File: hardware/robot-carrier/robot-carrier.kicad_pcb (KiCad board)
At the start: 2 copper layers, 65.5 x 73.5 mm, 36 parts, among them J1 DB128L BAT IN, LCSC C500021, J10 M1, J11 M2, J12 M3, J13 M4, J2 DB128L 2P, LCSC C500021, J20 S1, J21 S2, J22 S3, J23 S4, J3 DB128L 2P, LCSC C500021, J30 IMU I2C, J40 GA25-370 L298N: ENA / IN1 / I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, J41 DB128L 3P, LCSC C430602

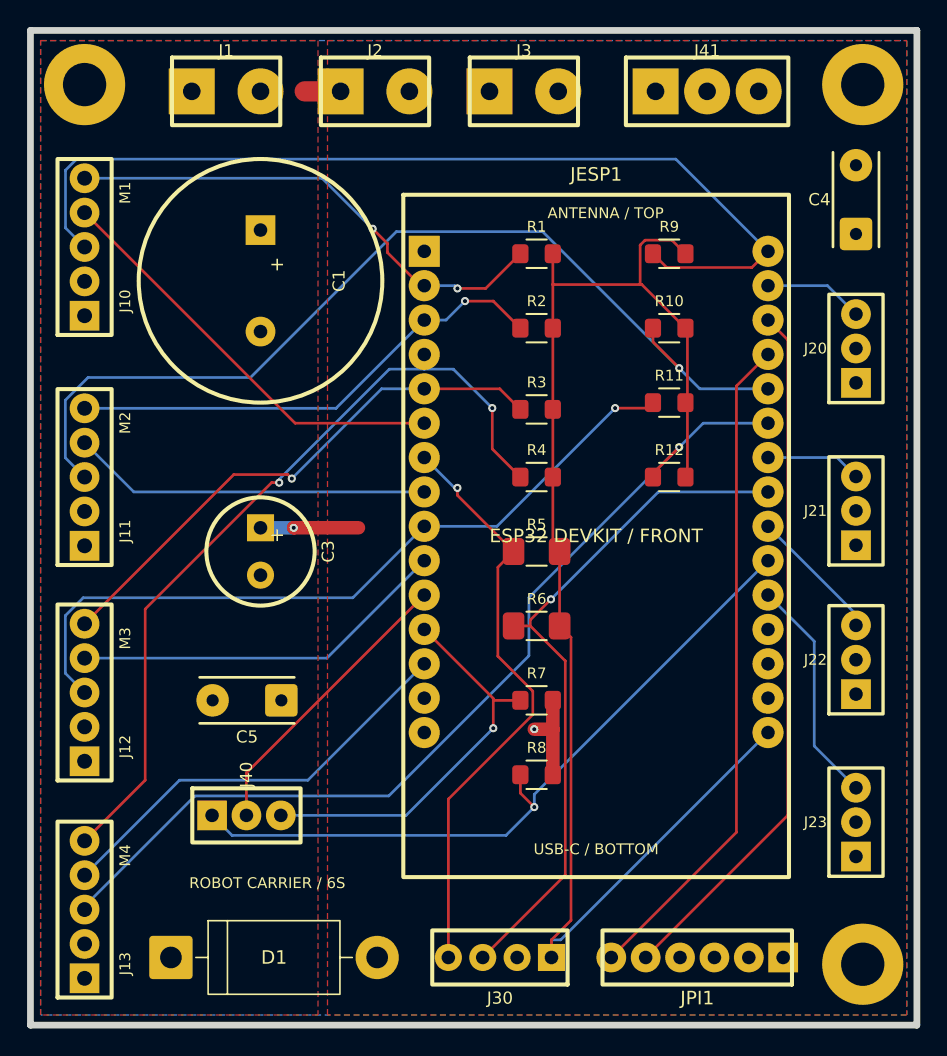
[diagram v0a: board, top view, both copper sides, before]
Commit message: Route carrier board with 1mm power and ground
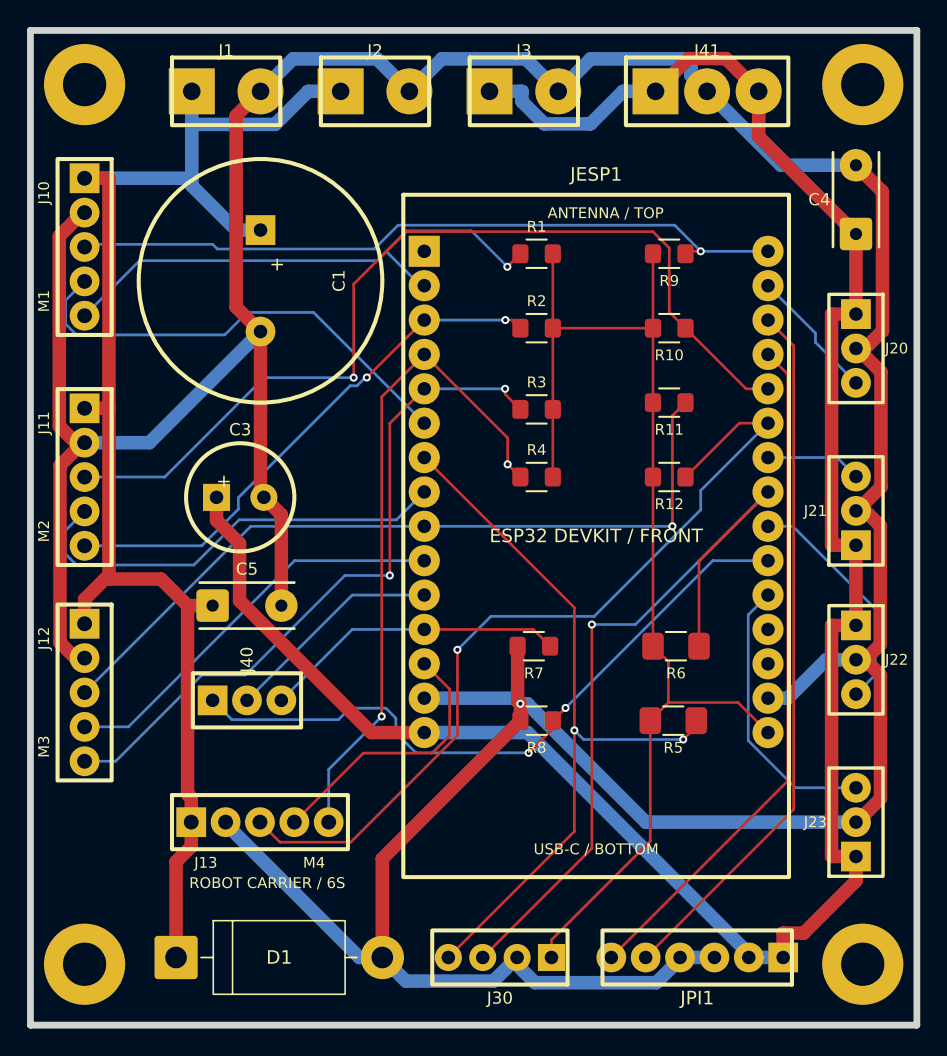
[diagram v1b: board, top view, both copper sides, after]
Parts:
- added H4: M3, Custom:MountingHole_M3, F.Cu at (24.0, 89.0)
- moved R5 16.1 mm to (67.5, 71.0), turned to 180 degrees
- moved J13 14.5 mm to (37.0, 78.5), turned to 0 degrees
- moved R6 10.4 mm to (67.7, 65.5), turned to 180 degrees
- moved J40 8.50 mm to (36.0, 69.5)
- moved C5 7.00 mm to (36.0, 62.5), turned to 0 degrees
- moved C3 4.27 mm to (35.5, 54.5), turned to 0 degrees
- moved R7 4.00 mm to (57.2, 65.5), turned to 180 degrees
- moved R8 4.00 mm to (57.4, 71.0), turned to 180 degrees
- moved D1 0.38 mm to (30.8, 88.5)
- turned J10 to -90 degrees
- turned J11 to -90 degrees
- turned J12 to -90 degrees
- turned J20 to -90 degrees
- turned J22 to -90 degrees
- turned R10 to 180 degrees
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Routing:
- net GND: track 6.87 -> 315.2 mm
- net +5V: track 7.24 -> 161.2 mm, vias 1 -> 0
- net VIN_PROTECTED: track 2.65 -> 105.8 mm
- net +3V3: track 106.0 -> 88.2 mm
- net M1_PWM_3V3: track 70.7 -> 53.5 mm, vias 0 -> 1
- net IMU_I2C_SDA_3V3: track 43.9 -> 55.5 mm, vias 1 -> 2
- net M4_DIR_3V3: track 31.6 -> 20.2 mm
- net M4_ENC: track 60.3 -> 49.5 mm
- net M3_ENC: track 40.3 -> 51.1 mm, vias 1 -> 2
- net M4_PWM_3V3: track 71.1 -> 63.3 mm
- net S3_PWM: track 10.0 -> 17.3 mm
- net IMU_I2C_SCL_3V3: track 51.3 -> 58.5 mm
- net GA25_IN2_3V3: track 29.8 -> 22.5 mm, vias 1 -> 0
- net M2_DIR_3V3: track 26.6 -> 32.8 mm
- net GA25_IN1_3V3: track 21.7 -> 16.3 mm
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- removed copper zone on F.Cu, net +5V
- removed copper zone on B.Cu, net GND
- removed copper zone on F.Cu, net VIN_PROTECTED

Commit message: updated to none cropper pour
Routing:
- net M4_ENC: vias 2 -> 1
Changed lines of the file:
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@@
 			(at 0 -3 0)
 			(layer "F.SilkS")
+			(hide yes)
 			(effects
 				(font
@@
 			(at 0 -3 0)
 			(layer "F.SilkS")
+			(hide yes)
 			(effects
 				(font
@@
 		)
 		(duplicate_pad_numbers_are_jumpers no)
-		(fp_rect
-			(start -4 -2.5)
-			(end 4 2.5)
-			(stroke
-				(width 0.3)
-				(type default)
-			)
-			(fill no)
-			(layer "F.SilkS")
-		)
 		(pad "1" thru_hole rect
 			(at -2.54 0)
@@
 			(at 0 -3 0)
 			(layer "F.SilkS")
+			(hide yes)
 			(effects
 				(font
@@
 		)
 		(duplicate_pad_numbers_are_jumpers no)
-		(fp_rect
-			(start -4 -2.5)
-			(end 4 2.5)
-			(stroke
-				(width 0.3)
-				(type default)
-			)
-			(fill no)
-			(layer "F.SilkS")
-		)
 		(pad "1" thru_hole rect
 			(at -2.54 0)
@@
 			(at 0 -3 0)
 			(layer "F.SilkS")
+			(hide yes)
 			(effects
 				(font
@@
 			(at 0 -3 0)
 			(layer "F.SilkS")
+			(hide yes)
 			(effects
 				(font
@@
 			(at 0 -3 0)
 			(layer "F.SilkS")
+			(hide yes)
 			(effects
 				(font
@@
 		)
 		(duplicate_pad_numbers_are_jumpers no)
-		(fp_rect
-			(start -4 -2.5)
-			(end 4 2.5)
-			(stroke
-				(width 0.3)
-				(type default)
-			)
-			(fill no)
-			(layer "F.SilkS")
-		)
 		(pad "1" thru_hole rect
 			(at -2.54 0)
@@
 			(layer "F.SilkS")
 		)
-		(fp_rect
-			(start -14.5 -22.21)
-			(end 14.5 28.71)
-			(stroke
-				(width 0.05)
-				(type default)
-			)
-			(fill no)
-			(layer "F.CrtYd")
-		)
 		(fp_text user "USB-C / BOTTOM"
 			(at 0 26.4 0)
@@
 			(at 0 -3 0)
 			(layer "F.SilkS")
+			(hide yes)
 			(effects
 				(font
@@
 		)
 		(fp_text user "+"
-			(at -1.2 -1.2 0)
+			(at -1.2 -2.7 0)
 			(layer "F.SilkS")
 			(effects
@@
 		)
 		(duplicate_pad_numbers_are_jumpers no)
-		(fp_rect
-			(start -7 -2)
-			(end 7 2)
-			(stroke
-				(width 0.3)
-				(type default)
-			)
-			(fill no)
-			(layer "F.SilkS")
-		)
 		(pad "1" thru_hole rect
 			(at -6.35 0 90)
@@
 			(at 0 -3 90)
 			(layer "F.SilkS")
+			(hide yes)
 			(effects
 				(font
@@
 			(at 0 -3 0)
 			(layer "F.SilkS")
+			(hide yes)
 			(effects
 				(font
@@
 		(size 0.6)
 		(drill 0.3)
-		(layers "F.Cu" "B.Cu")
-		(net "M4_ENC")
-	)
-	(via
-		(at 55.2597 52.0597)
-		(size 0.6)
-		(drill 0.3)

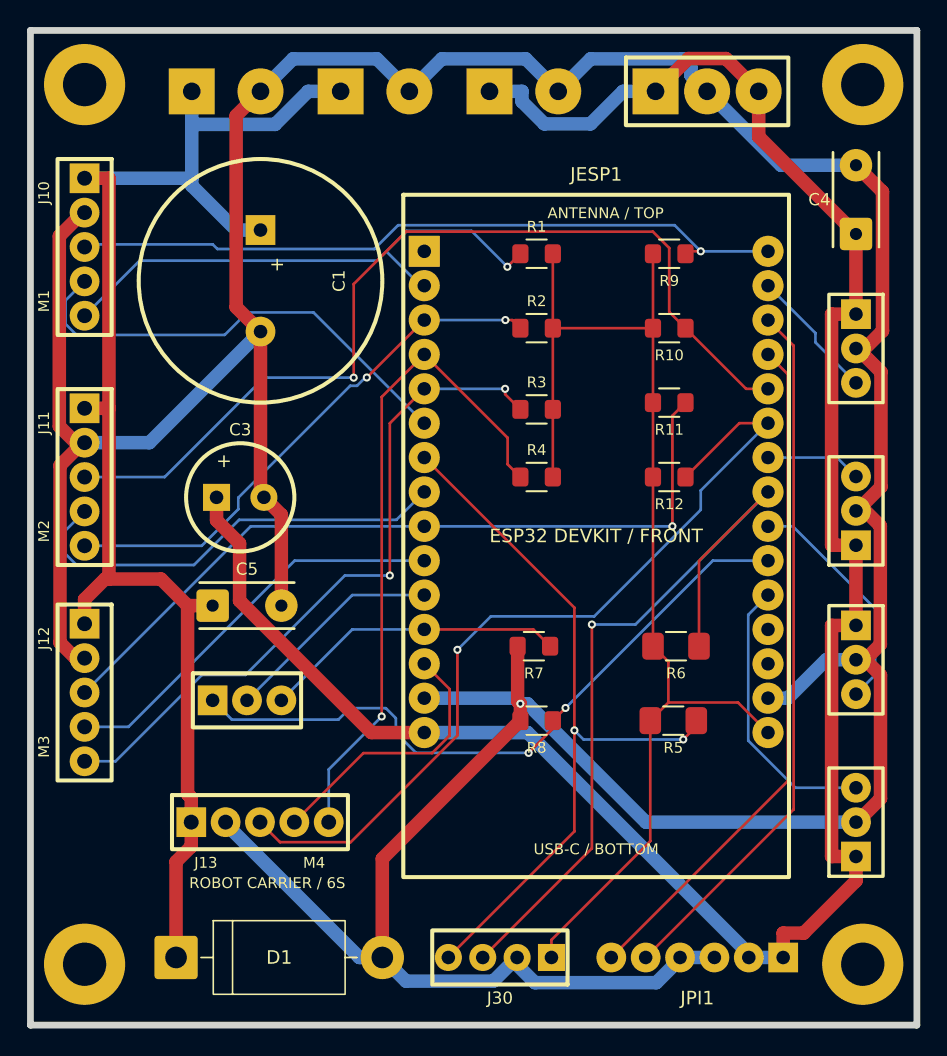
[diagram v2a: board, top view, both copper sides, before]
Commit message: Reroute carrier board
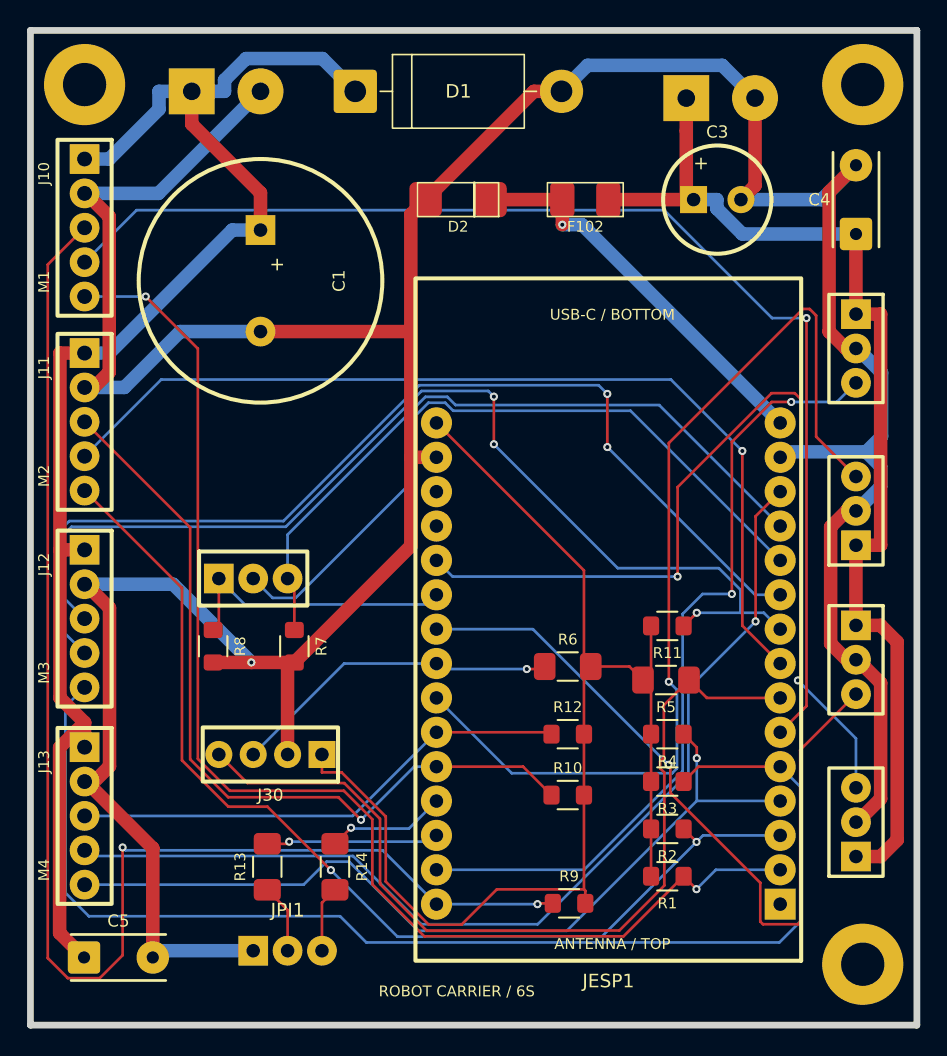
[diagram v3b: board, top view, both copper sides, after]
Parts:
- removed H4: M3, Custom:MountingHole_M3
- removed J2: DB128L 2P, LCSC C500021, Custom:TERM_BLOCK_1X02
- removed J41: DB128L 3P, LCSC C430602, Custom:TERM_BLOCK_1X03
- added D2: SMAJ5.0A, Diode_SMD:D_SMA, F.Cu at (51.6, 32.5)
- added F102: PPTC 0.75A 6V, Fuse:Fuse_1812_4532Metric, F.Cu at (61.0, 32.5)
- added R13: 470R Pi TX -> ESP RX, Custom:R_1206_HAND, F.Cu at (37.5, 81.8)
- added R14: 470R ESP TX -> Pi RX, Custom:R_1206_HAND, F.Cu at (42.5, 81.8)
- JPI1: value RPI4B REMOTE: 5V / GND / UART -> RPI4B UART: GND / TX / RX; footprint Custom:PI_REMOTE_1X06_MALE -> Custom:DUPONT_MALE_1X03
- moved D1 65.4 mm to (44.0, 24.5)
- moved R9 48.6 mm to (59.8, 84.5), turned to 0 degrees
- moved R1 47.0 mm to (67.1, 82.5), turned to 180 degrees
- moved C3 41.6 mm to (70.8, 32.5)
- moved R2 38.2 mm to (67.1, 79.0), turned to 180 degrees
- moved R10 35.3 mm to (59.7, 76.5), turned to 0 degrees
- moved JPI1 30.3 mm to (39.0, 88.0), turned to 0 degrees
- moved R3 29.1 mm to (67.1, 75.5), turned to 180 degrees
- moved C5 27.7 mm to (26.5, 88.5)
- moved R8 24.5 mm to (33.5, 65.5), turned to -90 degrees
- moved J30 22.6 mm to (37.7, 73.5)
- moved R4 21.3 mm to (67.1, 72.0), turned to 180 degrees
- moved R12 20.4 mm to (59.7, 72.0), turned to 0 degrees
- moved R7 17.7 mm to (39.5, 65.5), turned to -90 degrees
- moved R11 16.5 mm to (67.1, 64.0)
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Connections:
- JESP1 pad 15: +5V -> +5V_ESP_PROTECTED
- JESP1 pad 18: PI_UART_TX_3V3 -> ESP_UART_RX_3V3
- JESP1 pad 19: PI_UART_RX_3V3 -> ESP_UART_TX_3V3
- JPI1 pad 1: +5V -> GND
- JPI1 pad 2: +5V -> PI_UART_TX_3V3
- JPI1 pad 3: GND -> PI_UART_RX_3V3
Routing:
- net +5V: track 161.2 -> 81.5 mm
- net S2_PWM: track 7.08 -> 72.8 mm, vias 0 -> 1
- net M1_DIR_3V3: track 34.6 -> 89.6 mm, vias 0 -> 1
- net M4_DIR_3V3: track 20.2 -> 75.1 mm, vias 0 -> 1
- net M1_ENC: track 40.1 -> 94.4 mm, vias 1 -> 2
- net M1_PWM_3V3: track 53.5 -> 103.5 mm, vias 1 -> 2
- net S1_PWM: track 9.87 -> 59.3 mm, vias 0 -> 2
- net PI_UART_TX_3V3: track 52.4 -> 5.12 mm
- net S4_PWM: track 20.8 -> 67.7 mm, vias 0 -> 2
- net M3_DIR_3V3: track 30.2 -> 76.3 mm, vias 0 -> 2
- net PI_UART_RX_3V3: track 50.6 -> 4.90 mm
- net M3_ENC: track 51.1 -> 91.9 mm, vias 2 -> 0
- net S3_PWM: track 17.3 -> 57.3 mm, vias 0 -> 1
- net GND: track 315.2 -> 275.5 mm
- net M2_DIR_3V3: track 32.8 -> 70.0 mm, vias 0 -> 1
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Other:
- board text removed: "ESP32 DEVKIT / FRONT"

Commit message: cropper pour
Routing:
- added copper zone on B.Cu, net GND
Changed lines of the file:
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@@
 		(net "PI_UART_RX_3V3")
+	)
+	(zone
+		(net "GND")
+		(layer "B.Cu")
+		(hatch edge 0.5)
+		(connect_pads
+			(clearance 0.2)
+		)
+		(min_thickness 0.25)
+		(fill yes
+			(thermal_gap 0.5)
+			(thermal_bridge_width 0.5)
+			(island_removal_mode 0)
+		)
+		(polygon
+			(pts
+				(xy 20.5 20.5) (xy 85 20.5) (xy 85 93) (xy 20.5 93)
+			)
+		)
 	)
 	(embedded_fonts no)
